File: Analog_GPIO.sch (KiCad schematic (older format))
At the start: 7 parts

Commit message: Added USB Host and Device
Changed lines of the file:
@@
 AIN4
 Wire Wire Line
-	1975 1875 2250 1875
-Wire Wire Line
-	2250 1875 2525 1875
+	1975 1875 2525 1875
 Wire Wire Line
 	2525 1775 2250 1775
 Wire Wire Line
-	2250 1675 2250 1775
-Wire Wire Line
-	2250 1775 2250 1875
+	2250 1675 2250 1875
 Connection ~ 2250 1875
 Wire Wire Line
@@
 	1375 2350 1375 2425
 Wire Wire Line
-	1375 2725 1375 2775
+	1375 2725 1375 2825
 Wire Wire Line
-	1375 2775 1375 2825
-Wire Wire Line
-	1375 2775 1675 2775
-Wire Wire Line
-	1675 2775 2525 2775
+	1375 2775 2525 2775
 Connection ~ 1375 2775
 Wire Wire Line
@@
 Connection ~ 1675 2775
 Wire Wire Line
-	1375 3125 1375 3200
-Wire Wire Line
-	1375 3200 1375 3275
+	1375 3125 1375 3275
 Wire Wire Line
 	1375 3200 1675 3200

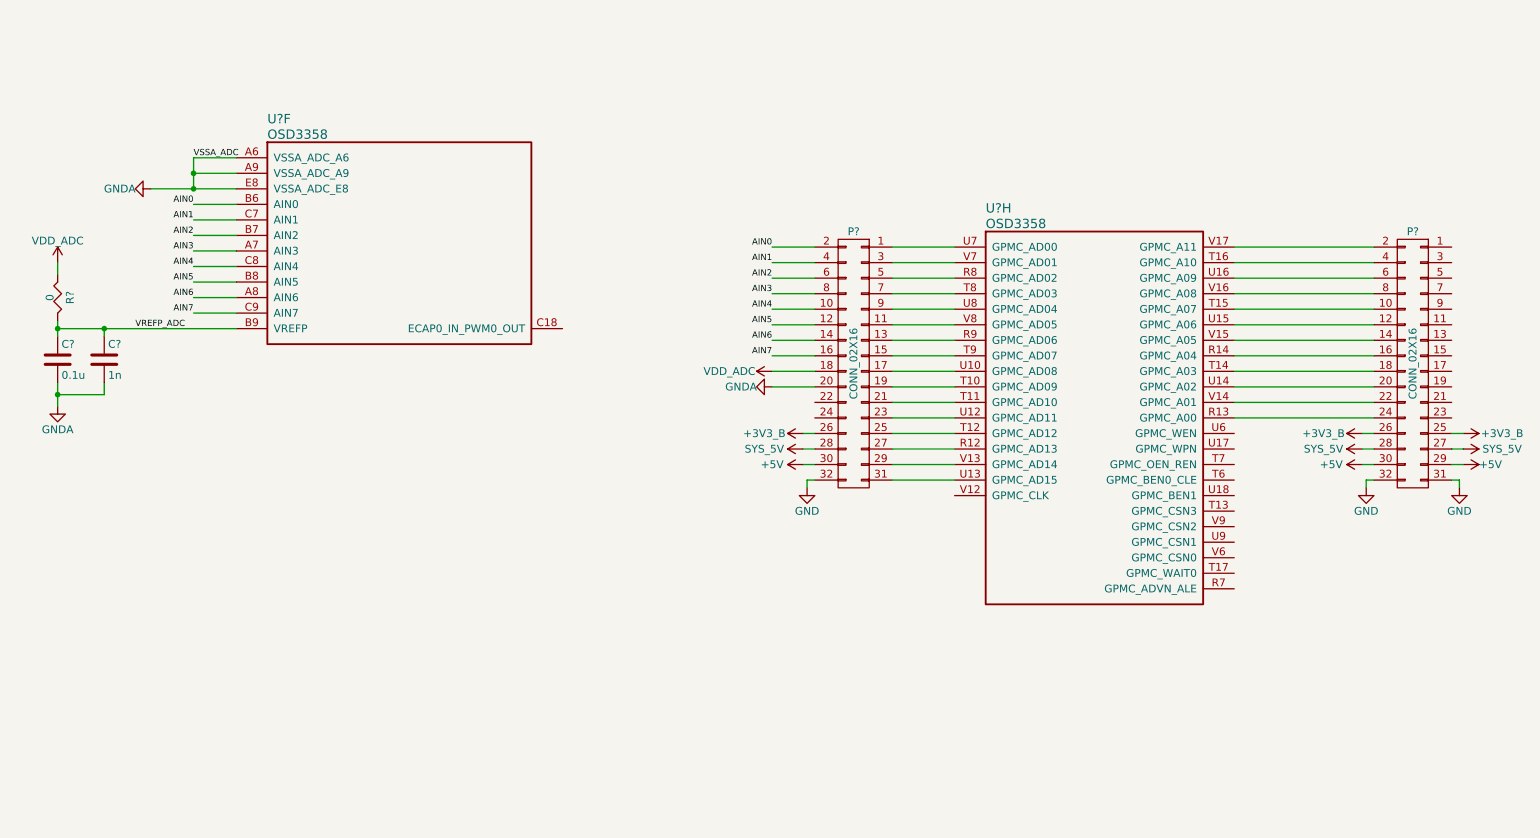
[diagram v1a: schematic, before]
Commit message: Added Sysboot configuration, user LEDs, updated README
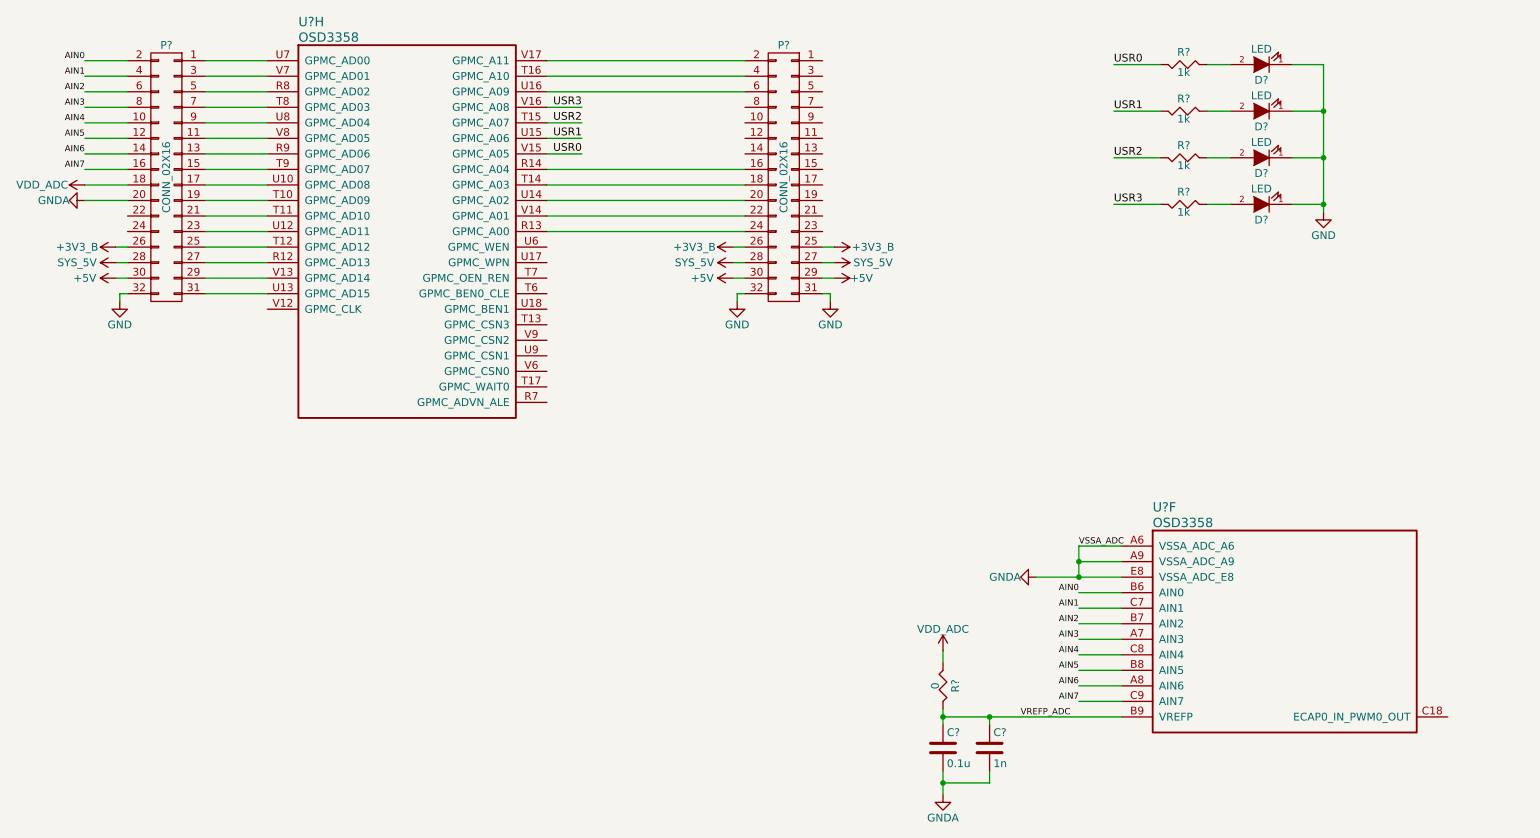
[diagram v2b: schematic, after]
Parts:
- added D? (x4): LED, symbol LED
- added R? (x4): 1k, symbol R
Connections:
- net GND: now also D?.1 (K), D?.1 (K), D?.1 (K), D?.1 (K)
- net at P?.10 (P10): no longer U?.T15 (GPMC_A07)
- net at P?.12 (P12): no longer U?.U15 (GPMC_A06)
- net at P?.14 (P14): no longer U?.V15 (GPMC_A05)
- net at P?.8 (P8): no longer U?.V16 (GPMC_A08)
- new net: D?.2 (A), R?.2 (x4)
- new net USR0: R?.1, U?.V15 (GPMC_A05)
- new net USR1: R?.1, U?.U15 (GPMC_A06)
- new net USR2: R?.1, U?.T15 (GPMC_A07)
- new net USR3: R?.1, U?.V16 (GPMC_A08)
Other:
- moved on the sheet: C?, P?, R?, U?F, U?H
